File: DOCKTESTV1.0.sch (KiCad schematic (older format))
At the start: 12 parts, among them J1 USB3_A, J3 bateria, J4 TB_1X2, P1N1 SW_PUSH, P2N1 SW_PUSH

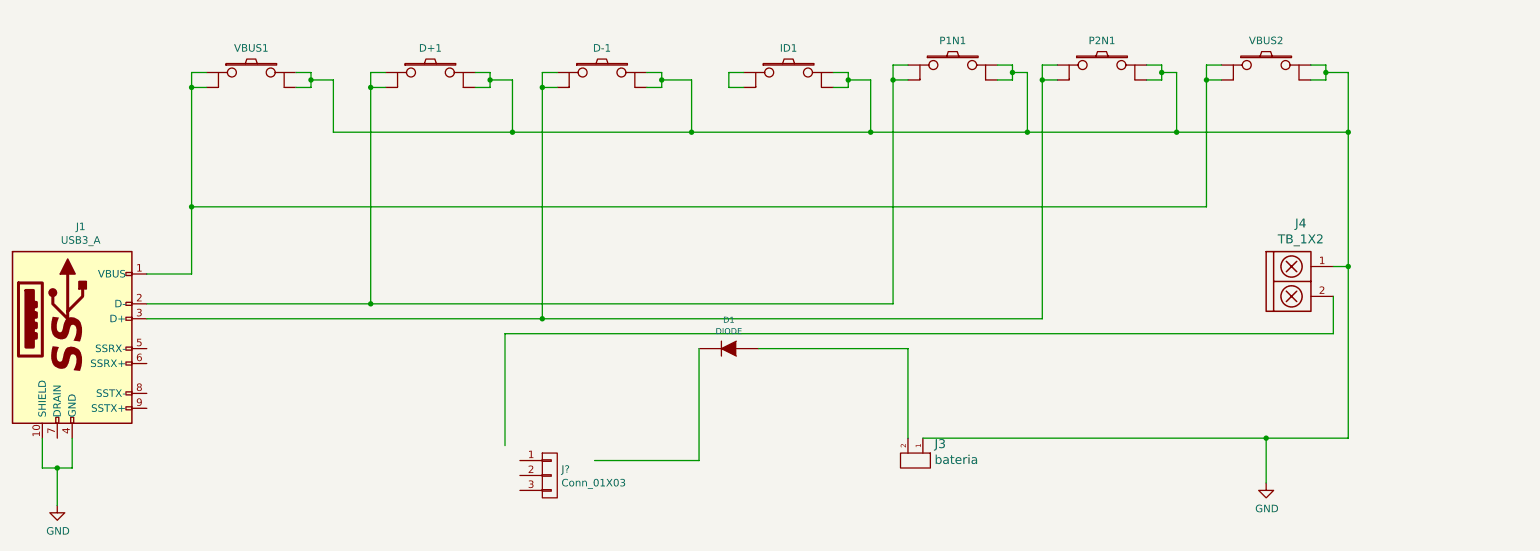
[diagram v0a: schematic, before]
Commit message: modificacion en el sch,pcb
se modifico una linea de gnd en el pcb y tambien se empezo el ruteo del pcb
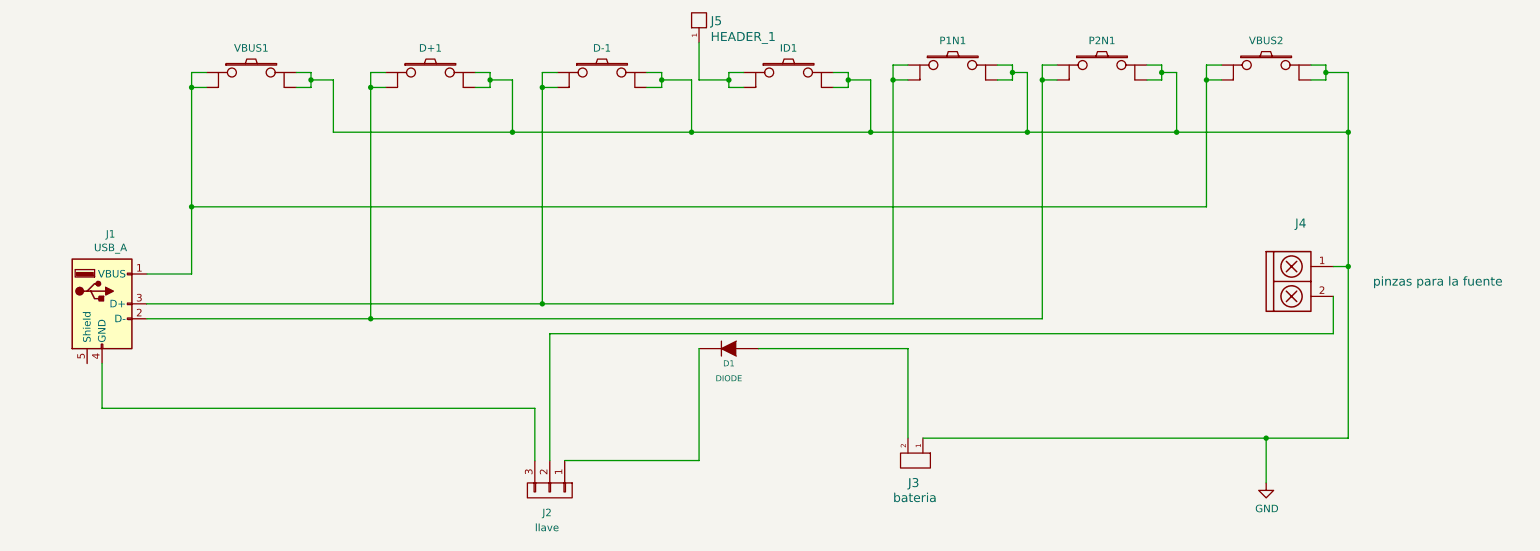
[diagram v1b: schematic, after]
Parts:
- removed J1: USB3_A, symbol Connector:USB3_A
- added J1: USB_A, Connector_USB:USB_A_Stewart_SS-52100-001_Horizontal, symbol Connector:USB_A
- added J5: HEADER_1, EESTN5:Cable_1,5mm, symbol EESTN5:HEADER_1
- J2: renamed from J?; value Conn_01X03 -> llave; footprint (none) -> EESTN5:Pin_Strip_3
- J4: value TB_1X2 -> pinzas para la fuente
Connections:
- net at VBUS1.1, VBUS1.2, VBUS2.1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: now also J1.1 (VBUS)
- net at D+1.1, D+1.2: now also P2N1.1, P2N1.2, J1.2 (D-); no longer P1N1.1, P1N1.2
- net at D-1.1, D-1.2: now also P1N1.1, P1N1.2, J1.3 (D+); no longer P2N1.1, P2N1.2
- net at ID1.1, ID1.2: now also J5.1
- net at D1.2 (K): now also J2.1 (P1)
- net at J4.2: now also J2.2 (P2)
- net at J2.3 (P3): now also J1.4 (GND)
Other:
- moved on the sheet: J2
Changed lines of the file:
@@
 EESchema Schematic File Version 4
+LIBS:DOCKTESTV1.0-cache
 EELAYER 30 0
 EELAYER END
@@
 $EndDescr
 $Comp
-L Connector:USB3_A J1
-U 1 1 60E4A8F8
-P 1450 3900
-F 0 "J1" H 1507 4617 50  0000 C CNN
-F 1 "USB3_A" H 1507 4526 50  0000 C CNN
-F 2 "" H 1600 4000 50  0001 C CNN
-F 3 "~" H 1600 4000 50  0001 C CNN
-	1    1450 3900
-	1    0    0    -1
-$EndComp
-$Comp
 L EESTN5:SW_PUSH D-1
 U 1 1 60E4CFCB
@@
 U 1 1 60E51976
 P 7100 4700
-F 0 "J3" V 7039 4828 60  0000 L CNN
-F 1 "bateria" V 7145 4828 60  0000 L CNN
+F 0 "J3" V 7300 4650 60  0000 L CNN
+F 1 "bateria" V 7400 4550 60  0000 L CNN
 F 2 "Battery:BatteryHolder_Keystone_500" H 7100 4950 60  0001 C CNN
 F 3 "" H 7100 4950 60  0000 C CNN
@@
 U 1 1 60E51C5A
 P 5850 4000
-F 0 "D1" H 5850 3808 40  0000 C CNN
-F 1 "DIODE" H 5850 3884 40  0000 C CNN
+F 0 "D1" H 5850 4100 40  0000 C CNN
+F 1 "DIODE" H 5850 4200 40  0000 C CNN
 F 2 "EESTN5:DO-41" H 5850 4000 60  0001 C CNN
 F 3 "" H 5850 4000 60  0000 C CNN
@@
 P 9550 3550
 F 0 "J4" H 9682 3939 60  0000 C CNN
-F 1 "TB_1X2" H 9682 3833 60  0000 C CNN
+F 1 "pinzas para la fuente" H 10600 3550 60  0000 C CNN
 F 2 "EESTN5:BORNERA2_DUO" H 9500 3600 60  0001 C CNN
 F 3 "" H 9500 3600 60  0000 C CNN
@@
 $EndComp
 Wire Wire Line
-	4950 4750 5650 4750
-Wire Wire Line
 	5650 4750 5650 4000
 Wire Wire Line
@@
 	7050 4000 6050 4000
 Wire Wire Line
-	4350 4650 4350 3900
-Wire Wire Line
-	4350 3900 9900 3900
-Wire Wire Line
 	9900 3900 9900 3650
 Wire Wire Line
@@
 Wire Wire Line
 	10000 4600 9450 4600
-Wire Wire Line
-	1450 4600 1450 4800
-Wire Wire Line
-	1450 4800 1350 4800
-Wire Wire Line
-	1250 4800 1250 4600
-Wire Wire Line
-	1350 4800 1350 5050
-Connection ~ 1350 4800
-Wire Wire Line
-	1350 4800 1250 4800
-$Comp
-L power:GND #PWR0101
-U 1 1 60E56FA0
-P 1350 5050
-F 0 "#PWR0101" H 1350 4800 50  0001 C CNN
-F 1 "GND" H 1355 4877 50  0000 C CNN
-F 2 "" H 1350 5050 50  0001 C CNN
-F 3 "" H 1350 5050 50  0001 C CNN
-	1    1350 5050
-	1    0    0    -1
-$EndComp
 Wire Wire Line
 	9450 4600 9450 4900
@@
 	5950 2250 5850 2250
 Wire Wire Line
-	5850 2250 5850 2150
+	5850 2250 5850 2200
 Wire Wire Line
 	5850 2150 5950 2150
@@
 Connection ~ 9050 2200
 Wire Wire Line
-	3450 3700 3450 2250
-Wire Wire Line
-	1950 3700 3450 3700
+	1950 3800 3450 3800
+Wire Wire Line
+	6950 2200 6950 3700
+Connection ~ 6950 2200
+Wire Wire Line
+	7950 3800 7950 2200
+Connection ~ 7950 2200
+$Comp
+L EESTN5:Conn_01X03 J2
+U 1 1 60E998D8
+P 4650 4950
+F 0 "J2" V 4800 4900 50  0000 L CNN
+F 1 "llave" V 4900 4850 50  0000 L CNN
+F 2 "EESTN5:Pin_Strip_3" H 4650 4950 50  0001 C CNN
+F 3 "" H 4650 4950 50  0001 C CNN
+	1    4650 4950
+	0    1    1    0
+$EndComp
+$Comp
+L Connector:USB_A J1
+U 1 1 60E66684
+P 1650 3700
+F 0 "J1" H 1707 4167 50  0000 C CNN
+F 1 "USB_A" H 1707 4076 50  0000 C CNN
+F 2 "Connector_USB:USB_A_Stewart_SS-52100-001_Horizontal" H 1800 3650 50  0001 C CNN
+F 3 " ~" H 1800 3650 50  0001 C CNN
+	1    1650 3700
+	1    0    0    -1
+$EndComp
+Wire Wire Line
+	1950 3700 4600 3700
+Wire Wire Line
+	3450 2250 3450 3800
 Connection ~ 3450 2250
-Wire Wire Line
-	4600 2250 4600 3800
-Wire Wire Line
-	1950 3800 4600 3800
+Connection ~ 3450 3800
+Wire Wire Line
+	3450 3800 7950 3800
+Wire Wire Line
+	4600 2250 4600 3700
 Connection ~ 4600 2250
-Wire Wire Line
-	6950 2200 6950 3700
-Wire Wire Line
-	6950 3700 3450 3700
-Connection ~ 6950 2200
-Connection ~ 3450 3700
-Wire Wire Line
-	4600 3800 7950 3800
-Wire Wire Line
-	7950 3800 7950 2200
-Connection ~ 4600 3800
-Connection ~ 7950 2200
-$Comp
-L EESTN5:Conn_01X03 J?
-U 1 1 60E998D8
-P 4650 4850
-F 0 "J?" H 4728 4891 50  0000 L CNN
-F 1 "Conn_01X03" H 4728 4800 50  0000 L CNN
-F 2 "" H 4650 4850 50  0001 C CNN
-F 3 "" H 4650 4850 50  0001 C CNN
-	1    4650 4850
-	1    0    0    -1
-$EndComp
+Connection ~ 4600 3700
+Wire Wire Line
+	4600 3700 6950 3700
+Wire Wire Line
+	4650 4750 4650 3900
+Wire Wire Line
+	4650 3900 9900 3900
+Wire Wire Line
+	4750 4750 5650 4750
+Wire Wire Line
+	4550 4750 4550 4400
+$Comp
+L EESTN5:HEADER_1 J5
+U 1 1 60E87DF4
+P 5650 1850
+F 0 "J5" V 5695 1772 60  0000 R CNN
+F 1 "HEADER_1" V 5589 1772 60  0000 R CNN
+F 2 "EESTN5:Cable_1,5mm" H 5650 2100 60  0001 C CNN
+F 3 "" H 5650 2100 60  0000 C CNN
+	1    5650 1850
+	0    -1   -1   0
+$EndComp
+Wire Wire Line
+	5650 1950 5650 2200
+Wire Wire Line
+	5650 2200 5850 2200
+Connection ~ 5850 2200
+Wire Wire Line
+	5850 2200 5850 2150
+Wire Wire Line
+	1650 4100 1650 4400
+Wire Wire Line
+	1650 4400 4550 4400
 $EndSCHEMATC
